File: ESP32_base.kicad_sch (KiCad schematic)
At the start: 40 parts, among them J1 Conn_01x16_Socket, J2 Conn_01x16_Socket, J5 KH-IPEXA-SMAKWE-B080H, SW1 boot, SW2 reset, U1 ADT7310TRZ, U2 AP63203WU-7, U3 ESP32-C5-WROOM-1U-N8-R8, U4 MCP23017-E/SO

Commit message: wip: battery
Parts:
- added C14, C15: 4.7uF, Capacitor_SMD:C_0805_2012Metric, symbol PCM_JLCPCB-Capacitors:0805,4.7uF
- added CN1: 530480210, easyeda2kicad:CONN-TH_530480210, symbol easyeda2kicad:530480210
- added D1: charging, LED_SMD:LED_0805_2012Metric, symbol Device:LED
- added R13: 470, Resistor_SMD:R_0805_2012Metric, symbol Device:R
- added R14: 2k, Resistor_SMD:R_0805_2012Metric, symbol Device:R
- added U5: MCP73831T-2ACI/OT, easyeda2kicad:SOT-23-5_L3.0-W1.7-P0.95-LS2.8-BL, symbol easyeda2kicad:MCP73831T-2ACI_OT
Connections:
- net +5V: now also C14.1, R13.2, U5.4 (VDD)
- net GND: now also C14.2, C15.2, CN1.2, R14.2, U5.2 (VSS)
- new net: D1.1 (K), U5.1 (STAT)
- new net: D1.2 (A), R13.1
- new net: R14.1, U5.5 (PROG)
- new net +BATT: C15.1, CN1.1, U5.3 (VBAT)
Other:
- note added: "battery: 802030 (8x20x30mm)"

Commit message: wip: battery
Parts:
- added D2: C426863, Diode_SMD:D_SOD-323, symbol easyeda2kicad:CUS10S30,H3F
- added Q1: AO3401A, Package_TO_SOT_SMD:SOT-23, symbol easyeda2kicad:AO3401A
- added R15: 100k, Resistor_SMD:R_0805_2012Metric, symbol Device:R
- R14: value 2k -> 2.5k
- U4: value MCP23017-E/SO -> MCP23017
- U5: value MCP73831T-2ACI/OT -> MCP73831T
- renumbered D1 to LED2
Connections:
- net +5V: now also D2.2 (A); no longer C4.2, U2.2 (EN), U2.3 (IN)
- net GND: now also R15.2
- net GPB6: no longer U4.7 (GPB6)
- net GPB7: no longer U4.8 (GPB7)
- net +BATT renamed VBAT
- net VBAT: now also Q1.2 (S)
- new net: Q1.1 (G), R15.1
- new net VSYS: C4.2, D2.1 (K), Q1.3 (D), U2.2 (EN), U2.3 (IN)
- no-connect marks 15 -> 17
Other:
- note added: "5V USB INPUT"
- note added: "TO AP63203WU-7"
- note added: "VIN: 4-32V, VOUT: 3.3V/2A"
- note added: "VIN: 5V & VBAT, VOUT: V_SYS"
- note added: "When running on Battery only (No USB): Gate (Pin 1): Pulled to GND by R15 (100kΩ). Source (Pin 2): Connected to VBAT (~3.7V). Result: The Gate is much lower than the Source, so the MOSFET turns ON. When USB is plugged in (+5V present): Source (Pin 2): Still at VBAT (~3.7V). Drain (Pin 3): Connected to VSYS, which is now being fed ~4.7V from the USB through the Schottky diode (D2). Result: The vol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"
- note added: "charge power"
- note removed: "3.3V / 2A (VIN: 4-32V)"
- moved on the sheet: AE1, C10, C11, C12, C13, C14, C15, C4, C5, C6, C7, C8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

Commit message: wip: pre solid pads
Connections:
- net GPB6: now also U4.7 (GPB6)
- net GPB7: now also U4.8 (GPB7)
- no-connect marks 17 -> 15
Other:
- note added: "ESP32 BT/WiFi base"
- note removed: "ESP32 Bluetooth LR base"
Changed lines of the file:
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@@
 		)
 	)
-	(text "ESP32 Bluetooth LR base"
-		(exclude_from_sim no)
-		(at 240.03 38.608 0)
+	(text "ESP32 BT/WiFi base"
+		(exclude_from_sim no)
+		(at 240.03 29.718 0)
 		(effects
 			(font
 				(size 7.62 7.62)
+				(thickness 1.524)
+				(bold yes)
 			)
 		)
@@
 	(text "When running on Battery only (No USB):\n  Gate (Pin 1): Pulled to GND by R15 (100kΩ).\n  Source (Pin 2): Connected to VBAT (~3.7V).\n  Result: The Gate is much lower than the Source, so the MOSFET turns ON.\n\nWhen USB is plugged in (+5V present):\n  Source (Pin 2): Still at VBAT (~3.7V).\n  Drain (Pin 3): Connected to VSYS, which is now being fed ~4.7V from the USB through the Schottky diode (D2).\n  Result: The voltage on both sides of the MOSFET is now high, the Gate-to-Source voltage difference disappears. \n  The MOSFET turns OFF, physically disconnecting the battery from the system rail so the USB can take over."
 		(exclude_from_sim no)
-		(at 180.34 60.706 0)
+		(at 180.34 58.674 0)
 		(effects
 			(font
@@
 	)
 	(no_connect
-		(at 377.19 309.88)
-	)
-	(no_connect
 		(at 377.19 292.1)
 	)
@@
 	)
 	(no_connect
-		(at 377.19 307.34)
-	)
-	(no_connect
 		(at 242.57 290.83)
 	)
@@
 	(wire
 		(pts
+			(xy 373.38 307.34) (xy 377.19 307.34)
+		)
+		(stroke
+			(width 0)
+			(type default)
+		)
+	)
+	(wire
+		(pts
 			(xy 406.4 312.42) (xy 402.59 312.42)
 		)
@@
 		)
 		(stroke
+			(width 0)
+			(type default)
+		)
+	)
+	(wire
+		(pts
+			(xy 373.38 309.88) (xy 377.19 309.88)
+		)
+		(stroke

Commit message: wip: INA219
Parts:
- added INA219: INA219AIDR, easyeda2kicad:SOIC-8_L4.9-W3.9-P1.27-LS6.0-BL, symbol easyeda2kicad:INA219AIDR
- added U7: 50m, easyeda2kicad:R1206, symbol easyeda2kicad:FRM121WFR050TM
- CN1: value 530480210 -> BATT CONN
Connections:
- net +3.3V: now also INA219.5 (VS)
- net GND: now also C4.2, INA219.1 (A1), INA219.2 (A0), INA219.6 (GND); no longer C4.1
- net SCL: now also INA219.4 (SCL)
- net SDA: now also INA219.3 (SDA)
- net VSYS: now also C4.1, INA219.7 (VIN-), U7.2; no longer C4.2, D2.1 (K), Q1.3 (D)
- new net VSOURCE: D2.1 (K), INA219.8 (VIN+), Q1.3 (D), U7.1
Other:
- note added: "+5V: charge power"
- note added: "5V: VBUS"
- note added: "POWER MEASUREMENT"
- note added: "VIN: 5V/VBAT, VOUT: VSOURCE"
- note added: "VIN: VSOURCE, VOUT: 3.3V"
- note added: "battery WidthHeightLength: move to 802035 (8mm thick, 20 mm wide, 25 mm. long) When running on Battery only (No USB): Gate (Pin 1): Pulled to GND by R15 (100kΩ). Source (Pin 2): Connected to VBAT (~3.7V). Result: The Gate is much lower than the Source, so the MOSFET turns ON. When USB is plugged in (+5V present): Source (Pin 2): Still at VBAT (~3.7V). Drain (Pin 3): Connected to VSYS, which is no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"
- note added: "battery: 102035"
- note removed: "5V USB INPUT"
- note removed: "VIN: 5V & VBAT, VOUT: V_SYS"
- note removed: "When running on Battery only (No USB): Gate (Pin 1): Pulled to GND by R15 (100kΩ). Source (Pin 2): Connected to VBAT (~3.7V). Result: The Gate is much lower than the Source, so the MOSFET turns ON. When USB is plugged in (+5V present): Source (Pin 2): Still at VBAT (~3.7V). Drain (Pin 3): Connected to VSYS, which is now being fed ~4.7V from the USB through the Schottky diode (D2). Result: The vol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"
- note removed: "battery: 802030 (8x20x30mm)"
- note removed: "charge power"
- moved on the sheet: AE1, C1, C11, C2, C3, C4, C5, C6, C7, FB1, FB2, J1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

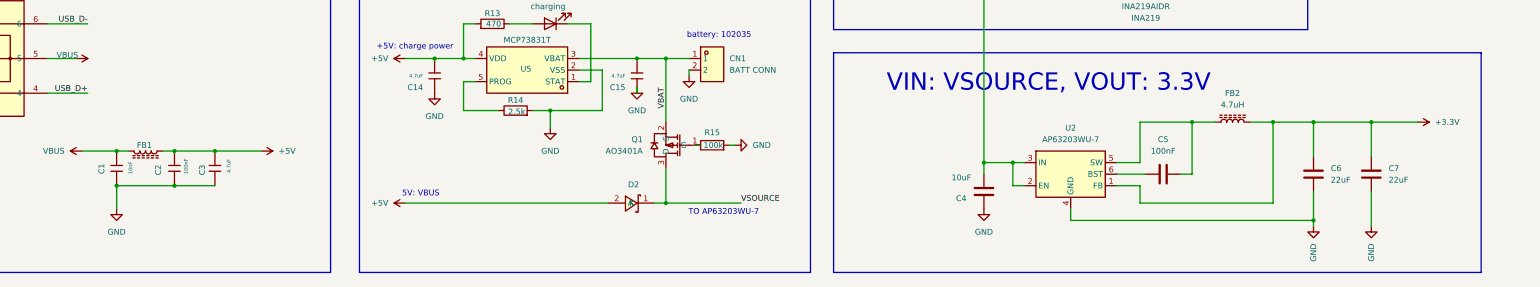
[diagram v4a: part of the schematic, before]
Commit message: angle via traces
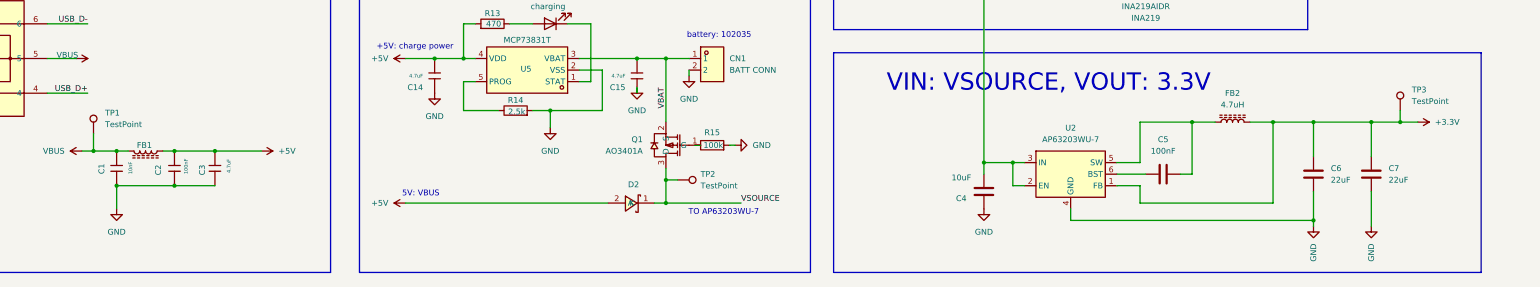
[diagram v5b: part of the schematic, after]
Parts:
- added TP1, TP2, TP3: TestPoint, TestPoint:TestPoint_Pad_D1.0mm, symbol Connector:TestPoint
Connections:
- net +3.3V: now also TP3.1
- net VBUS: now also TP1.1
- net VSOURCE: now also TP2.1

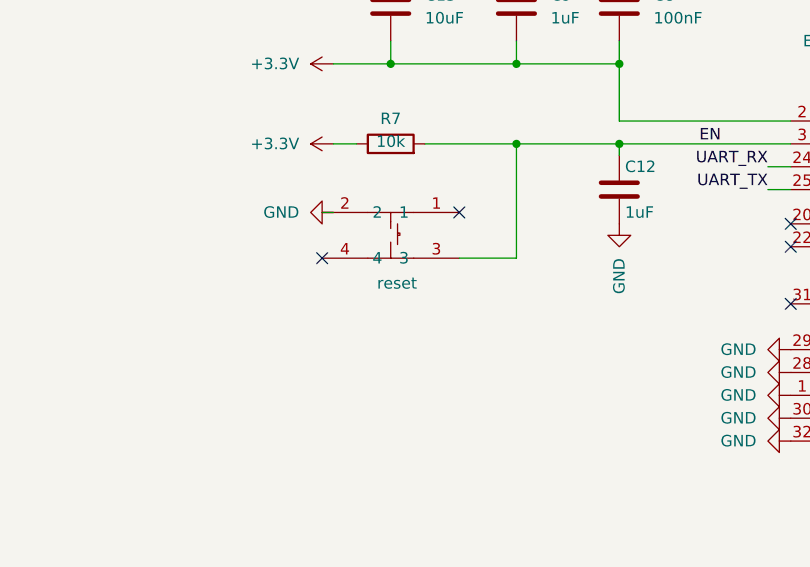
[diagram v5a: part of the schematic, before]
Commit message: button: reset -> mode
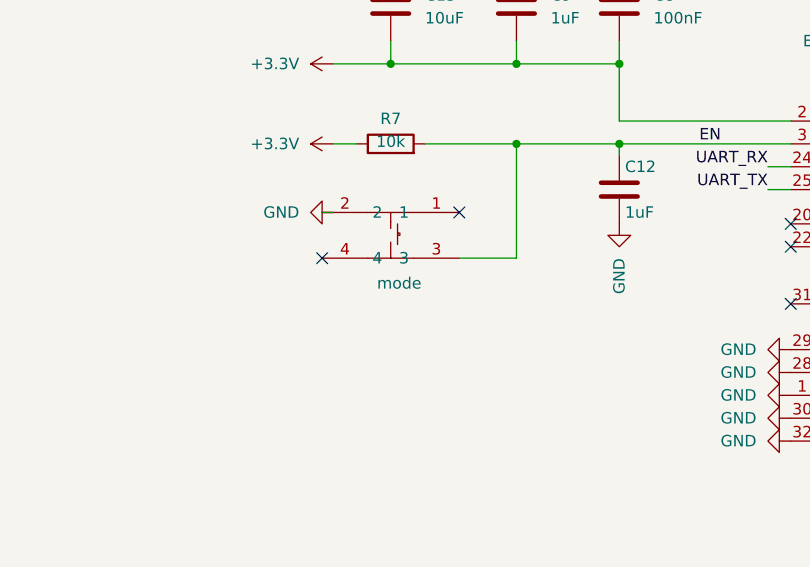
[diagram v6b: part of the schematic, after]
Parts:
- SW2: value reset -> mode
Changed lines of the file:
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@@
 			)
 		)
-		(property "Value" "reset"
+		(property "Value" "mode"
 			(at 196.596 297.434 0)
 			(effects

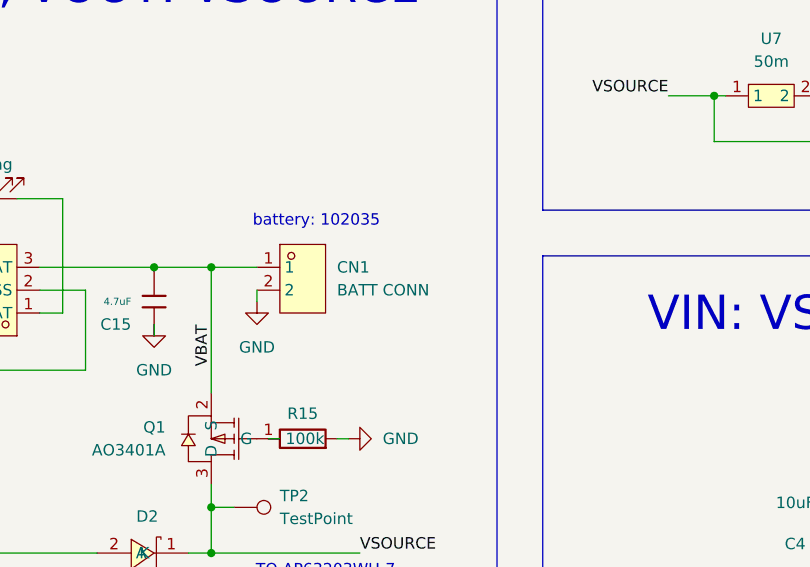
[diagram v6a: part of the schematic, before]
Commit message: use new battery connector
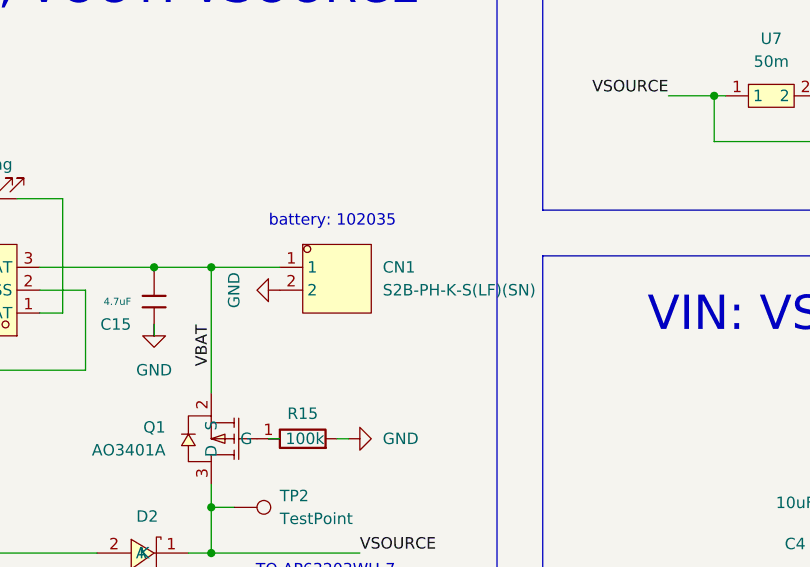
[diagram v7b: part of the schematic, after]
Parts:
- removed CN1: BATT CONN, easyeda2kicad:CONN-TH_530480210, symbol easyeda2kicad:530480210
- added CN1: S2B-PH-K-S(LF)(SN), easyeda2kicad:CONN-TH_S2B-PH-K-S-LF-SN, symbol easyeda2kicad:S2B-PH-K-S(LF)(SN)
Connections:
- net GND: now also CN1.2
- net VBAT: now also CN1.1
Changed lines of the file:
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@@
 	(text "battery: 102035"
 		(exclude_from_sim no)
-		(at 259.334 102.87 0)
+		(at 261.112 102.87 0)
 		(effects
 			(font
@@
 	(wire
 		(pts
-			(xy 247.65 107.95) (xy 252.73 107.95)
+			(xy 247.65 107.95) (xy 255.27 107.95)
 		)
 		(stroke
@@
 	(wire
 		(pts
-			(xy 252.73 111.76) (xy 252.73 110.49)
-		)
-		(stroke
-			(width 0)
-			(type default)
-		)
-	)
-	(wire
-		(pts
 			(xy 361.95 304.8) (xy 377.19 304.8)
 		)
@@
 	)
 	(symbol
-		(lib_id "easyeda2kicad:530480210")
-		(at 257.81 109.22 0)
+		(lib_id "easyeda2kicad:S2B-PH-K-S(LF)(SN)")
+		(at 260.35 109.22 0)
 		(unit 1)
 		(exclude_from_sim no)
@@
 		(fields_autoplaced yes)
 		(property "Reference" "CN1"
-			(at 261.62 107.9499 0)
+			(at 266.7 107.9499 0)
 			(effects
 				(font
@@
 			)
 		)
-		(property "Value" "BATT CONN"
-			(at 261.62 110.4899 0)
+		(property "Value" "S2B-PH-K-S(LF)(SN)"
+			(at 266.7 110.4899 0)
 			(effects
 				(font
@@
 			)
 		)
-		(property "Footprint" "easyeda2kicad:CONN-TH_530480210"
-			(at 257.81 118.11 0)
-			(effects
-				(font
-					(size 1.27 1.27)
-				)
-				(hide yes)
-			)
-		)
-		(property "Datasheet" "https://lcsc.com/product-detail/Wire-To-Board-Wire-To-Wire-Connector_MOLEX-530480210_C505099.html"
-			(at 257.81 120.65 0)
+		(property "Footprint" "easyeda2kicad:CONN-TH_S2B-PH-K-S-LF-SN"
+			(at 260.35 118.11 0)
 			(effects
 				(font
@@
 			)
 		)
-		(property "Description" "Connector Header 2 position 1.25mm Pitch 1A Right Angle -40℃~+85℃"
-			(at 257.81 109.22 0)
+		(property "Datasheet" "https://lcsc.com/product-detail/PH-Connectors_JST-Sales-America_S2B-PH-K-S-LF-SN_JST-Sales-America-S2B-PH-K-S-LF-SN_C173752.html"
+			(at 260.35 120.65 0)
 			(effects
 				(font
@@
 			)
 		)
-		(property "LCSC Part" "C505099"
-			(at 257.81 123.19 0)
+		(property "Description" ""
+			(at 260.35 109.22 0)
 			(effects
 				(font
@@
 			)
 		)
-		(property "Mfr. Part" "530480210"
-			(at 257.81 109.22 0)
+		(property "LCSC Part" "C173752"
+			(at 260.35 123.19 0)
 			(effects
 				(font
@@
 	(symbol
 		(lib_id "power:GND")
-		(at 252.73 111.76 0)
+		(at 255.27 110.49 270)
 		(unit 1)
 		(exclude_from_sim no)
@@
 		(fields_autoplaced yes)
 		(property "Reference" "#PWR056"
-			(at 252.73 118.11 0)
+			(at 248.92 110.49 0)
 			(effects
 				(font
@@
 		)
 		(property "Value" "GND"
-			(at 252.73 116.84 0)
+			(at 250.19 110.49 0)
 			(effects
 				(font
@@
 		)
 		(property "Footprint" ""
-			(at 252.73 111.76 0)
+			(at 255.27 110.49 0)
 			(effects
 				(font
@@
 		)
 		(property "Datasheet" ""
-			(at 252.73 111.76 0)
+			(at 255.27 110.49 0)
 			(effects
 				(font
@@
 		)
 		(property "Description" "Power symbol creates a global label with name \"GND\" , ground"
-			(at 252.73 111.76 0)
+			(at 255.27 110.49 0)
 			(effects
 				(font
@@
 		)
 		(instances
-			(project ""
+			(project "ESP32_base"
 				(path "/773fb1fd-83fe-4444-84df-dce6da829395"
 					(reference "#PWR056")
